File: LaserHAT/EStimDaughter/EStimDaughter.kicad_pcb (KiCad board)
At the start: 4 copper layers, 26.5 x 23.5 mm, 48 parts, among them J1 ELECTRODE E1/E2, J8 J8 power/timing (underside), J9 J9 analog/SPI (underside), U1 ISO7761FDBQR, U2 TLV76050DBZR, U3 TL431 (2.5V), U4 MCP4921-E/MS, U5 OPA2192IDGKR, U6 74HC4053PW, U7 DG419DY

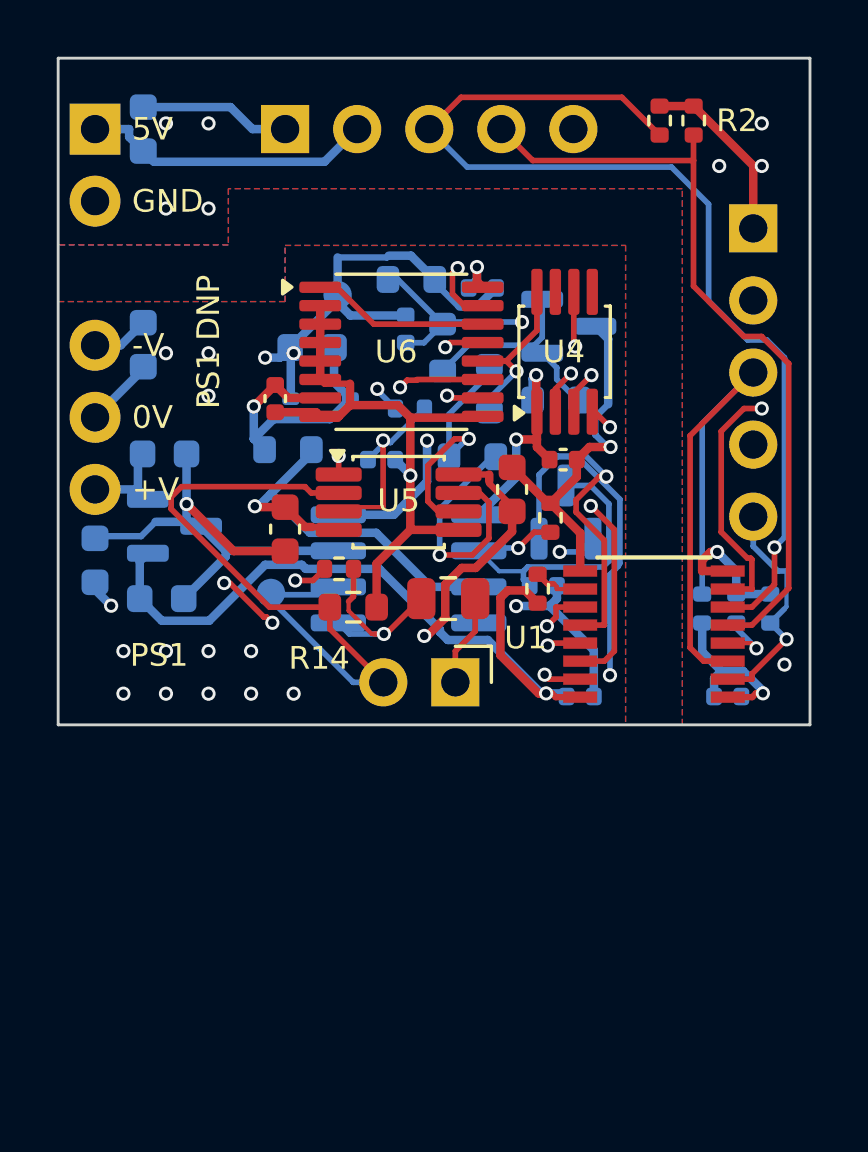
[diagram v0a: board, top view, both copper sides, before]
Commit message: EStimDaughter rev M3: fault detector restored, 26.5 x 36.5 mm single-sided board, DHVQFN 4053 + MSOP DG419B
- LM393 compliance / open-electrode window (U8, R20-R28, C18, C19) back exactly as in rev E;
  sim/fault.py + monitor() in sim/spice.py (LM2903B TI model): trips at |E1| > 0.915 V,
  7-12 us before the current collapses, open electrode in 3.8 us, no false trips.
- 74HC4053PW -> 74HC4053BQ (DHVQFN-16), DG419DY -> DG419BDQ (MSOP-8; 15 ohm, 38 pC, 12 pF).
- Module outline extended 12.5 mm south over the Pi's port edge (y 76-112.5, HAT NOTICE 12),
  all SMD on the top; HAT column ends at y 100 so the SE corner is isolated.
- tools: route_pcb/build_pcb/netcheck take FREEROUTING / KICAD_CLI / KICAD_FOOTPRINTS from
  the environment (Ubuntu); U8 anchored, single-sided placement; Freerouting seed 0 + fix-ups:
  DRC clean, 0 unconnected, netcheck OK.
- Docs: README, DESIGN_NOTES (M2/M3 sections), spec MCU pins (PA7/PA12/PA6/PA22) and outline,
  NOTICE 11 (fault detector) and 12 (outline), REV2_NOTES, BOM (57 lines), fab outputs.
- stash/: M1 and M2 boards for reference. EStimDaughter/route/ is git-ignored.

Co-Authored-By: Claude Fable 5.1 <noreply@anthropic.com>
Claude-Session: https://claude.ai/code/session_018vgLizGzYPynnY93ajvoVA
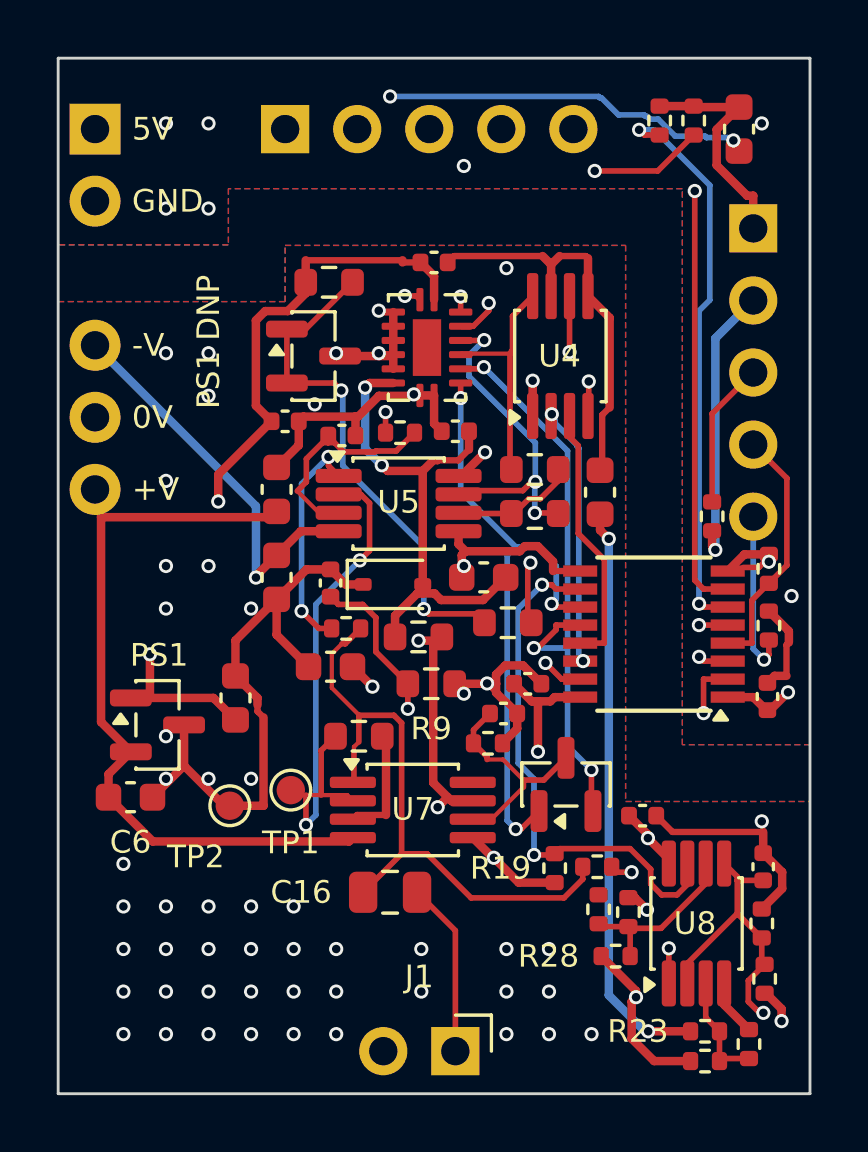
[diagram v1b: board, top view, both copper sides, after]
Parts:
- added C18: 100p, C_0402_1005Metric, F.Cu at (125.8, 104.5)
- added C19: 100n, C_0402_1005Metric, F.Cu at (117.5, 98.0)
- added R20: 100k, R_0402_1005Metric, F.Cu at (120.0, 104.5)
- added R21: 12k, R_0402_1005Metric, F.Cu at (125.8, 106.5)
- added R22: 27k, R_0402_1005Metric, F.Cu at (125.9, 108.5)
- added R23: 110k, R_0402_1005Metric, F.Cu at (123.8, 110.3)
- added R24: 12k, R_0402_1005Metric, F.Cu at (125.3, 110.8)
- added R25: 27k, R_0402_1005Metric, F.Cu at (123.8, 111.3)
- added R26: 110k, R_0402_1005Metric, F.Cu at (121.1, 106.1)
- added R27: 12k, R_0402_1005Metric, F.Cu at (120.0, 106.0)
- added R28: 27k, R_0402_1005Metric, F.Cu at (120.7, 107.7)
- added U8: LM393DGKR, VSSOP-8_3x3mm_P0.65mm, F.Cu at (123.5, 106.5)
- C1, C13, C15, C17, C2, C3, C4, C5, C6, C7, C8, C9, D1, D2, R10, R11, R12, R3, R4, R5, R6, R7, R8, R9, TP1, TP2, U2, U3: moved to F.Cu
- U6: value 74HC4053PW -> 74HC4053BQ; footprint TSSOP-16_4.4x5mm_P0.65mm -> DHVQFN-16-1EP_2.5x3.5mm_P0.5mm_EP1x2mm
- U7: value DG419DY -> DG419BDQ; footprint SOIC-8_3.9x4.9mm_P1.27mm -> MSOP-8_3x3mm_P0.65mm; moved to F.Cu
- moved C3 21.0 mm to (125.0, 78.5)
- moved TP2 18.4 mm to (107.0, 102.3)
- moved R9 14.3 mm to (114.2, 98.0)
- moved J1 13.0 mm to (115.0, 111.0)
- moved C6 12.2 mm to (103.5, 102.0)
- moved C16 10.6 mm to (112.7, 105.4)
- moved C8 10.1 mm to (116.0, 94.3)
- moved R8 9.97 mm to (116.8, 95.9), turned to 0 degrees
- moved C10 9.89 mm to (109.0, 88.8)
- moved R19 9.87 mm to (118.5, 104.5)
- moved D2 9.60 mm to (118.9, 101.6)
- moved C5 9.45 mm to (108.7, 94.3)
- moved C9 9.33 mm to (110.6, 94.5)
- moved U3 9.06 mm to (110.0, 86.5)
- moved R7 9.01 mm to (110.5, 83.9)
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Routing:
- net +5V_ISO: track 51.0 -> 99.3 mm, vias 4 -> 8
- net +V_STIM: track 40.4 -> 77.1 mm
- net CATH: track 50.3 -> 21.3 mm, vias 5 -> 3
- net FAULT_n: track 1.76 -> 26.2 mm, vias 0 -> 3
- net Net-(U8A--): track 0.00 -> 18.2 mm, vias 0 -> 2
- net -V_STIM: track 24.9 -> 41.1 mm, vias 1 -> 5
- net E1: track 6.73 -> 22.3 mm, vias 1 -> 0
- net +5V_H: track 10.4 -> 24.6 mm, vias 0 -> 2
- net Net-(U4-VREF): track 11.2 -> 24.7 mm, vias 2 -> 3
- net Net-(U3-K): track 7.98 -> 18.2 mm, vias 0 -> 2
- net EN_H: track 37.1 -> 28.7 mm, vias 1 -> 2
- net -5V_ISO: track 10.6 -> 17.9 mm, vias 1 -> 2
- net EN: track 15.3 -> 22.0 mm
- net CATH_H: track 27.7 -> 34.4 mm, vias 0 -> 2
- net Net-(U8B--): track 0.00 -> 6.18 mm
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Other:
- board size 26.5 x 23.5 mm -> 26.5 x 36.5 mm

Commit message: EStimDaughter rev M4: I2C DAC (DAC60501 via ISO1640), dedicated RELEASE line for the SHORT switch
- U1 ISO7761F -> ISO7741F (EN, CATH, RELEASE forward; FAULT_n back), new U9 ISO1640
  bidirectional I2C isolator.  J9.3/4/5 = RELEASE / SCL / SDA (HAT NOTICE 13); the HAT's
  copper does not change.
- MCP4921 + TL431 reference chain (U3, R7-R9, C9) -> DAC60501ZDGSR, I2C address 0x48,
  internal 2.5 V reference / 2 = 0-1.25 V; R14 2.00k -> 2.49k 0.1 % (502 uA full scale).
- Hold timer D2/R15/C17 removed: the DG419B is driven by RELEASE (low = shorted; fail-safe
  unchanged).  R3 = RELEASE pull-down, R7/R8 and R9/R15 = 4.7k I2C pull-ups.
- Schematic regenerated (netcheck OK, ERC 0); sims: VREF 1.25 V, R14 2.49k (set-point
  -0.28 %, mismatch -0.005 %).
- PCB: placed only (build_pcb + planes/pours; HAT column to y 106, U9 straddles below U1),
  NOT routed - hand routing follows.  Fab outputs are still the M3 set.
- Docs: README, DESIGN_NOTES (M4 section, firmware contract), spec, NOTICE 13, REV2_NOTES.

Co-Authored-By: Claude Fable 5.1 <noreply@anthropic.com>
Claude-Session: https://claude.ai/code/session_018vgLizGzYPynnY93ajvoVA
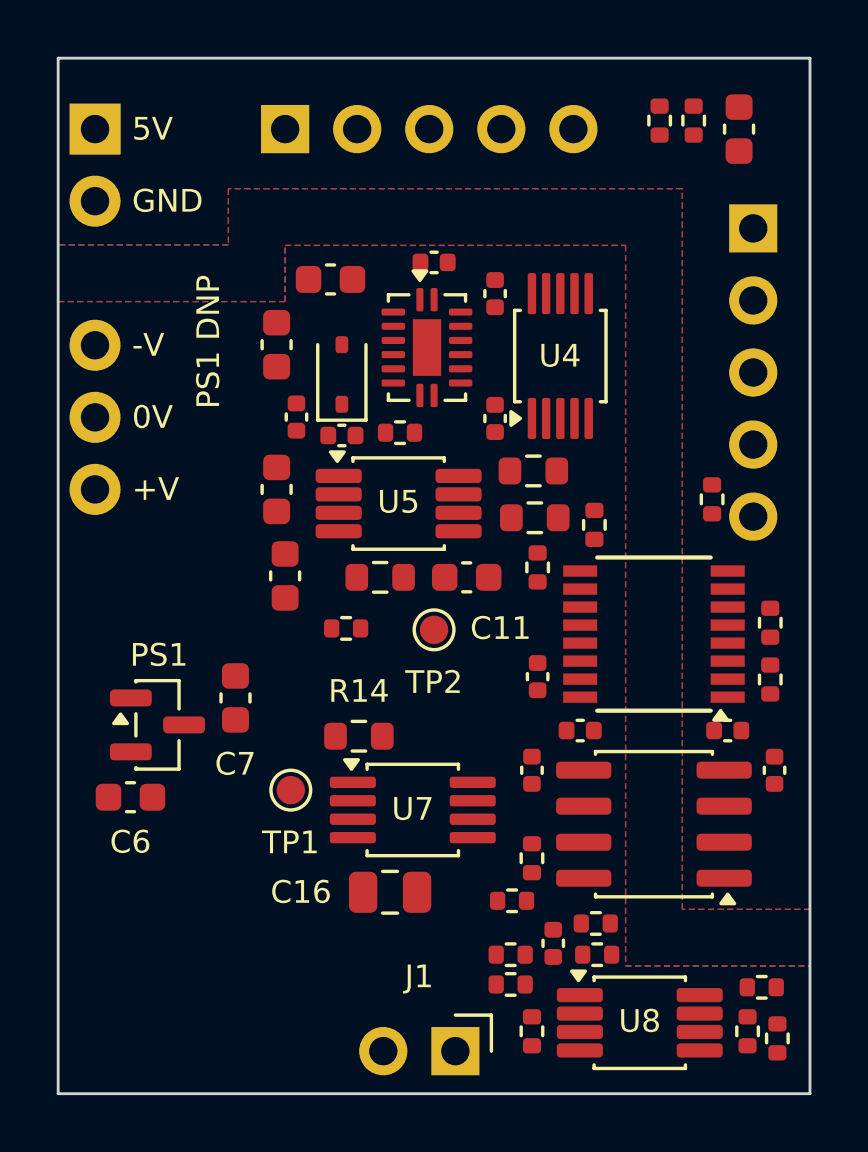
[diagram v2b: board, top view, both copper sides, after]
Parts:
- removed D2: BAT54C, SOT-23
- removed R4, R5: 100k, R_0402_1005Metric
- removed U3: TL431 (2.5V), SOT-23
- added C20: 100n, C_0402_1005Metric, F.Cu at (117.7, 101.1)
- added U9: ISO1640BDR, SOIC-8_3.9x4.9mm_P1.27mm, F.Cu at (122.0, 103.0)
- C17: value 2.2n -> 100n
- C9: value 10n -> 100n
- J9: value J9 analog/SPI (underside) -> J9 I2C/release (underside)
- R14: value 2.00k 0.1% -> 2.49k 0.1%
- R15: value 100k -> 4.7k
- R7: value 1.5k -> 4.7k; footprint R_0603_1608Metric -> R_0402_1005Metric
- R8: value 15.0k 0.1% -> 4.7k; footprint R_0603_1608Metric -> R_0402_1005Metric
- R9: value 10.0k 0.1% -> 4.7k; footprint R_0603_1608Metric -> R_0402_1005Metric
- U1: value ISO7761FDBQR -> ISO7741FDBQR
- U4: value MCP4921-E/MS -> DAC60501ZDGSR; footprint MSOP-8_3x3mm_P0.65mm -> VSSOP-10_3x3mm_P0.5mm
- moved R7 20.9 mm to (126.1, 97.9), turned to 90 degrees
- moved C8 11.8 mm to (110.6, 83.8)
- moved C9 11.7 mm to (116.4, 84.3)
- moved C17 9.76 mm to (126.2, 101.1), turned to 90 degrees
- moved TP2 9.50 mm to (114.2, 96.2)
- moved R8 9.25 mm to (126.1, 95.9), turned to 90 degrees
- moved R24 8.66 mm to (117.0, 108.7), turned to 0 degrees
- moved R15 8.56 mm to (119.9, 92.5), turned to 90 degrees
- moved C5 8.20 mm to (108.7, 86.1)
- moved C18 7.88 mm to (118.5, 107.2)
- moved R25 7.81 mm to (117.0, 107.6)
- moved R27 7.77 mm to (126.3, 110.5)
- moved D1 7.62 mm to (111.0, 87.2), turned to 90 degrees
- moved C10 7.40 mm to (116.4, 88.7), turned to 90 degrees
- moved R22 6.26 mm to (120.0, 106.5), turned to 0 degrees
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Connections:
- C17 pad 1: HOLD -> +3V3_H
- C17 pad 2: GND_ISO -> GND_H
- C9 pad 1: Net-(U4-VREF) -> Net-(U4-VREFIO)
- J9 pad 3: CS_H -> RELEASE_H
- J9 pad 4: SCK_H -> SCL_H
- J9 pad 5: MOSI_H -> SDA_H
- R15 pad 1: HOLD -> +5V_ISO
- R15 pad 2: GND_ISO -> SCL
- R3 pad 1: +3V3_H -> RELEASE_H
- R3 pad 2: CS_H -> GND_H
- R7 pad 1: +5V_ISO -> +3V3_H
- R7 pad 2: Net-(U3-K) -> SDA_H
- R8 pad 1: Net-(U3-K) -> +3V3_H
- R8 pad 2: Net-(U4-VREF) -> SCL_H
- R9 pad 1: Net-(U4-VREF) -> +5V_ISO
- R9 pad 2: GND_ISO -> SDA
- U1 pad 10: FAULT_n -> +5V_ISO
- U1 pad 11: EN -> FAULT_n
- U1 pad 12: CATH -> RELEASE
- U1 pad 13: SCK -> CATH
- U1 pad 14: CS_n -> EN
- U1 pad 15: MOSI -> GND_ISO
- U1 pad 2: MOSI_H -> GND_H
- U1 pad 3: CS_H -> EN_H
- U1 pad 4: SCK_H -> CATH_H
- U1 pad 5: CATH_H -> RELEASE_H
- U1 pad 6: EN_H -> FAULT_H
- U1 pad 7: FAULT_H -> +3V3_H
- U4 pad 2: CS_n -> Net-(U4-VOUT)
- U4 pad 3: SCK -> unconnected-(U4-NC-Pad3)
- U4 pad 4: MOSI -> GND_ISO
- U4 pad 5: GND_ISO -> +5V_ISO
- U4 pad 6: Net-(U4-VREF) -> SCL
- U4 pad 8: Net-(U4-VOUT) -> SDA
- U7 pad 6: HOLD -> RELEASE
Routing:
- net +5V_ISO: track 99.3 -> 0.00 mm, vias 8 -> 0
- net +V_STIM: track 77.1 -> 0.00 mm, vias 3 -> 0
- net GND_ISO: track 76.4 -> 0.00 mm, vias 55 -> 0
- net -V_STIM: track 41.1 -> 0.00 mm, vias 5 -> 0
- net CATH_H: track 34.4 -> 0.00 mm, vias 2 -> 0
- net EN_H: track 28.7 -> 0.00 mm, vias 2 -> 0
- net ISENSE: track 28.4 -> 0.00 mm, vias 2 -> 0
- net FAULT_n: track 26.2 -> 0.00 mm, vias 3 -> 0
- net Net-(U4-VREF): track 24.7 -> 0.00 mm, vias 3 -> 0
- net +5V_H: track 24.6 -> 0.00 mm, vias 2 -> 0
- net E1: track 22.3 -> 0.00 mm
- net EN: track 22.0 -> 0.00 mm, vias 3 -> 0
- net CATH: track 21.3 -> 0.00 mm, vias 3 -> 0
- net FAULT_H: track 20.2 -> 0.00 mm, vias 1 -> 0
- net +3V3_H: track 18.7 -> 0.00 mm, vias 2 -> 0
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
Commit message: EStimDaughter: L-shaped isolation barrier on all layers, isolator channels follow the placement, J9.4/J9.5 = SDA/SCL
- Barrier is now a plain L (y 83.58 to x 120, x 120 down to y 95.5, then east); GND_H / GND_ISO
  zones on F, In1, In2 and B share the same two outlines; rule areas ISOLATION_BARRIER_0/1/2.
- U1 ISO7741F channels A/B/C = RELEASE/CATH/EN so J8.3/J8.4 and J9.3 drop straight in. FAULT_n
  stays on J8.5: PA6 is the MCU's only TIMA0 fault pin (one via needed).
- J9.4 = SDA, J9.5 = SCL (spec section 7); U9 ISO1640 channels swapped with it so the DAC
  connects without crossings. HAT firmware change only (PA17 = SDA, PA22 = SCL); open question
  for the HAT session in LAYOUT_HANDOFF.md.
- Schematic regenerated (netcheck OK); DRC has no new violations.

Co-Authored-By: Claude Fable 5.1 <noreply@anthropic.com>
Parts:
- moved R11 38.8 mm to (156.6, 94.0)
- moved R12 38.8 mm to (151.8, 91.0)
- moved C10 38.8 mm to (155.2, 90.5)
- moved C11 38.8 mm to (154.2, 96.2)
- moved C12 38.8 mm to (147.8, 96.1)
- moved C14 38.8 mm to (148.2, 90.5)
- moved C15 38.8 mm to (149.8, 91.2)
- moved D1 38.8 mm to (149.8, 89.0)
- moved R10 38.8 mm to (156.5, 92.4)
- moved R13 38.8 mm to (149.9, 98.0)
- moved R6 38.8 mm to (151.1, 96.2)
- moved TP2 38.8 mm to (153.0, 98.0)
- moved U5 38.8 mm to (151.8, 93.5)
- moved U6 38.8 mm to (152.8, 88.0)
- moved C4 38.8 mm to (147.4, 93.0)
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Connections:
- J9 pad 4: SCL_H -> SDA_H
- J9 pad 5: SDA_H -> SCL_H
- U1 pad 12: RELEASE -> EN
- U1 pad 14: EN -> RELEASE
- U1 pad 3: EN_H -> RELEASE_H
- U1 pad 5: RELEASE_H -> EN_H
- U9 pad 2: SDA_H -> SCL_H
- U9 pad 3: SCL_H -> SDA_H
- U9 pad 6: SCL -> SDA
- U9 pad 7: SDA -> SCL
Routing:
- net RELEASE_H: track 0.00 -> 8.30 mm
- net +3V3_H: track 0.00 -> 6.85 mm
- net SCL_H: track 0.00 -> 1.75 mm, vias 0 -> 1
- net SDA_H: track 0.00 -> 1.66 mm, vias 0 -> 1
